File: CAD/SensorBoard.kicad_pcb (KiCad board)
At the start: 4 copper layers, 0 parts

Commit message: Begin initial PCB design
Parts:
- added C1: 4u7, Capacitor_SMD:C_0603_1608Metric, F.Cu at (112.5, 134.5)
- added C10: TODO, Capacitor_SMD:C_0402_1005Metric, F.Cu at (92.0, 134.2)
- added C11: TODO, Capacitor_SMD:C_0402_1005Metric, F.Cu at (92.0, 136.2)
- added C12: TODO, Capacitor_SMD:C_0402_1005Metric, F.Cu at (92.0, 138.2)
- added C13: TODO, Capacitor_SMD:C_0402_1005Metric, F.Cu at (92.0, 140.1)
- added C14: 100n, Capacitor_SMD:C_0402_1005Metric, F.Cu at (92.0, 142.1)
- added C15: 100n, Capacitor_SMD:C_0402_1005Metric, F.Cu at (94.8, 134.2)
- added C16: 100n, Capacitor_SMD:C_0402_1005Metric, F.Cu at (94.8, 136.2)
- added C17: 100n, Capacitor_SMD:C_0402_1005Metric, F.Cu at (94.8, 138.2)
- added C18: 100n, Capacitor_SMD:C_0402_1005Metric, F.Cu at (94.8, 140.1)
- added C19: 100n, Capacitor_SMD:C_0402_1005Metric, F.Cu at (94.8, 142.1)
- added C2: 4u7, Capacitor_SMD:C_0603_1608Metric, F.Cu at (112.5, 137.0)
- added C20: 100n, Capacitor_SMD:C_0402_1005Metric, F.Cu at (97.7, 134.2)
- added C21: 100n, Capacitor_SMD:C_0402_1005Metric, F.Cu at (97.7, 136.2)
- added C22: 100n, Capacitor_SMD:C_0402_1005Metric, F.Cu at (97.7, 138.2)
- added C23: 100n, Capacitor_SMD:C_0402_1005Metric, F.Cu at (97.7, 140.1)
- added C24: 100n, Capacitor_SMD:C_0402_1005Metric, F.Cu at (97.7, 142.1)
- added C3: 100n, Capacitor_SMD:C_0402_1005Metric, F.Cu at (89.1, 134.2)
- added C4: 100n, Capacitor_SMD:C_0402_1005Metric, F.Cu at (89.1, 136.2)
- added C5: 100n, Capacitor_SMD:C_0402_1005Metric, F.Cu at (89.1, 138.2)
- added C6: 100n, Capacitor_SMD:C_0402_1005Metric, F.Cu at (89.1, 140.1)
- added C7: 100n, Capacitor_SMD:C_0402_1005Metric, F.Cu at (89.1, 142.1)
- added C8: 4u7, Capacitor_SMD:C_0603_1608Metric, F.Cu at (112.5, 139.5)
- added C9: 4u7, Capacitor_SMD:C_0603_1608Metric, F.Cu at (112.5, 142.0)
- added D1: RED, LED_SMD:LED_0402_1005Metric, F.Cu at (167.0, 119.5)
- added D2: RED, LED_SMD:LED_0402_1005Metric, F.Cu at (169.0, 119.5)
- added D3: RED, LED_SMD:LED_0402_1005Metric, F.Cu at (171.0, 119.5)
- added D4: RED, LED_SMD:LED_0402_1005Metric, F.Cu at (173.0, 119.5)
- added D6: LED, LED_SMD:LED_0402_1005Metric, F.Cu at (144.0, 119.5)
- added D7: LED, LED_SMD:LED_0402_1005Metric, F.Cu at (144.0, 121.5)
- added D8: ASMT-YTB7-0AA02, LED_SMD:LED_Avago_PLCC6_3x2.8mm, F.Cu at (159.0, 121.5)
- added J1: USB C 2.0, Connector_USB:USB_C_Receptacle_GCT_USB4105-xx-A_16P_TopMnt_Horizontal, F.Cu at (126.8, 135.0)
- added J2: SWD Connector, SensorBoard:SM03B-SR, F.Cu at (186.9, 141.1)
- added J3: UART Connector, SensorBoard:SM03B-SR, F.Cu at (186.9, 129.0)
- added J4: DAC Connector, SensorBoard:SM02B-SR, F.Cu at (186.9, 135.0)
- added M1: M1, MountingHole:MountingHole_3.2mm_M3_Pad_Via, F.Cu at (128.5, 121.0)
- added M2: M2, MountingHole:MountingHole_3.2mm_M3_Pad_Via, F.Cu at (128.5, 149.0)
- added M3: M3, MountingHole:MountingHole_3.2mm_M3_Pad_Via, F.Cu at (186.5, 121.0)
- added M4: M4, MountingHole:MountingHole_3.2mm_M3_Pad_Via, F.Cu at (186.5, 149.0)
- added R1: TODO, Resistor_SMD:R_0402_1005Metric, F.Cu at (89.1, 118.3)
- added R10: 1k, Resistor_SMD:R_0402_1005Metric, F.Cu at (92.0, 120.3)
- added R11: TODO, Resistor_SMD:R_0402_1005Metric, F.Cu at (92.0, 122.3)
- added R12: 220, Resistor_SMD:R_0402_1005Metric, F.Cu at (92.0, 124.3)
- added R13: 5k1, Resistor_SMD:R_0402_1005Metric, F.Cu at (92.0, 126.3)
- added R14: 220, Resistor_SMD:R_0402_1005Metric, F.Cu at (92.0, 128.2)
- added R15: 220, Resistor_SMD:R_0402_1005Metric, F.Cu at (92.0, 130.2)
- added R16: 5k1, Resistor_SMD:R_0402_1005Metric, F.Cu at (92.0, 132.2)
- added R17: 220, Resistor_SMD:R_0402_1005Metric, F.Cu at (94.9, 118.3)
- added R18: 5k1, Resistor_SMD:R_0402_1005Metric, F.Cu at (94.9, 120.3)
- added R19: 220, Resistor_SMD:R_0402_1005Metric, F.Cu at (94.9, 122.3)
- added R2: TODO, Resistor_SMD:R_0402_1005Metric, F.Cu at (89.1, 120.3)
- added R20: 5k1, Resistor_SMD:R_0402_1005Metric, F.Cu at (94.9, 124.3)
- added R21: 220, Resistor_SMD:R_0402_1005Metric, F.Cu at (94.9, 126.3)
- added R22: 5k1, Resistor_SMD:R_0402_1005Metric, F.Cu at (94.9, 128.2)
- added R23: 220, Resistor_SMD:R_0402_1005Metric, F.Cu at (94.9, 130.2)
- added R24: 220, Resistor_SMD:R_0402_1005Metric, F.Cu at (94.9, 132.2)
- added R25: 220, Resistor_SMD:R_0402_1005Metric, F.Cu at (97.8, 118.3)
- added R26: 220, Resistor_SMD:R_0402_1005Metric, F.Cu at (97.8, 120.3)
- added R27: 220, Resistor_SMD:R_0402_1005Metric, F.Cu at (97.8, 122.3)
- added R28: 220, Resistor_SMD:R_0402_1005Metric, F.Cu at (97.8, 124.3)
- added R29: 220, Resistor_SMD:R_0402_1005Metric, F.Cu at (97.8, 126.3)
- added R3: 100, Resistor_SMD:R_0402_1005Metric, F.Cu at (89.1, 122.3)
- added R4: 100, Resistor_SMD:R_0402_1005Metric, F.Cu at (89.1, 124.3)
- added R5: 100, Resistor_SMD:R_0402_1005Metric, F.Cu at (89.1, 126.3)
- added R6: 100, Resistor_SMD:R_0402_1005Metric, F.Cu at (89.1, 128.2)
- added R7: 5k1, Resistor_SMD:R_0402_1005Metric, F.Cu at (89.1, 130.2)
- added R8: 5k1, Resistor_SMD:R_0402_1005Metric, F.Cu at (89.1, 132.2)
- added R9: 1k, Resistor_SMD:R_0402_1005Metric, F.Cu at (92.0, 118.3)
- added SW1: SW_1, Button_Switch_SMD:SW_Push_SPST_NO_Alps_SKRK, F.Cu at (155.1, 149.5)
- added SW2: SW_2, Button_Switch_SMD:SW_Push_SPST_NO_Alps_SKRK, F.Cu at (159.6, 149.5)
- added SW3: SW_3, Button_Switch_SMD:SW_Push_SPST_NO_Alps_SKRK, F.Cu at (164.0, 149.5)
- added SW4: SW_4, Button_Switch_SMD:SW_Push_SPST_NO_Alps_SKRK, F.Cu at (168.4, 149.5)
- added SW5: SW_BOOT, Button_Switch_SMD:SW_Push_SPST_NO_Alps_SKRK, F.Cu at (136.0, 126.0)
- added SW6: SW_RST, Button_Switch_SMD:SW_Push_SPST_NO_Alps_SKRK, F.Cu at (136.5, 143.5)
- added U1: STM32U073CCT6, Package_QFP:LQFP-48_7x7mm_P0.5mm, F.Cu at (160.0, 135.0)
- added U2: MIC5365, Package_TO_SOT_SMD:SOT-23-5, F.Cu at (147.1, 128.1)
- added U3: USBLC6-2SC6, Package_TO_SOT_SMD:SOT-23-6, F.Cu at (137.1, 135.0)
- added U4: BME680, SensorBoard:BME630, F.Cu at (173.0, 134.5)
- added U5: BMI323, SensorBoard:BMI323, F.Cu at (148.0, 135.5)
- added U6: TC1047, Package_TO_SOT_SMD:SOT-23, F.Cu at (172.1, 126.0)
- added X1: 32MHz, Crystal:Crystal_SMD_2016-4Pin_2.0x1.6mm, F.Cu at (169.8, 142.4)
- added X2: 32kHz768, Crystal:Crystal_SMD_2012-2Pin_2.0x1.2mm, F.Cu at (149.0, 142.5)
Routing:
- added copper zone on In1.Cu, net GND
- added copper zone on In2.Cu, net GND
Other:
- board outline added: 69.9 x 40 mm

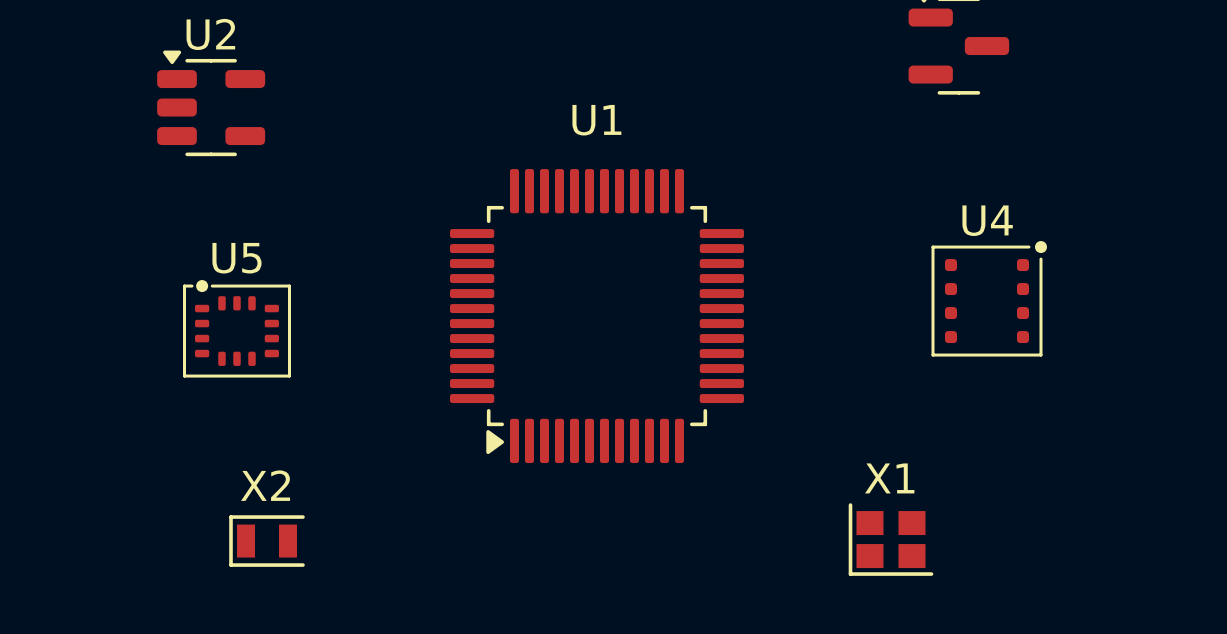
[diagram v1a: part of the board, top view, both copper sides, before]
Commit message: Add updates to footprints
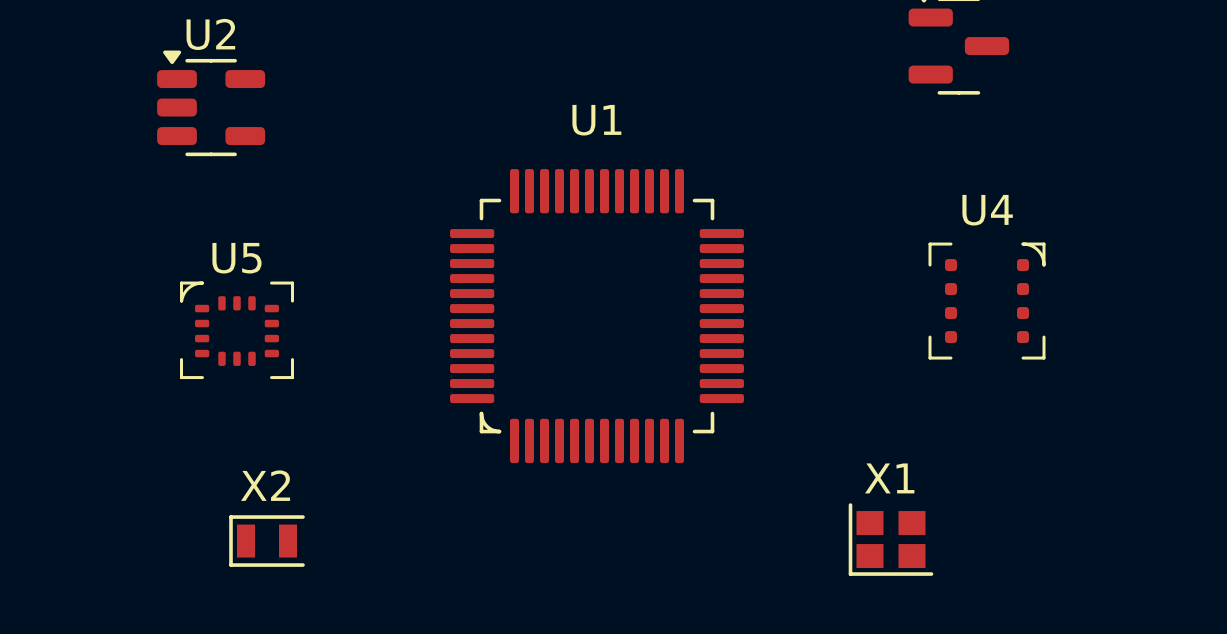
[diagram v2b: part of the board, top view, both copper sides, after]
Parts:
- U1: footprint Package_QFP:LQFP-48_7x7mm_P0.5mm -> SensorBoard:LQFP-48_7x7mm_P0.5mm
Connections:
- J1 pad A8: (no net) -> unconnected-(J1-SBU1-PadA8)
- J1 pad B8: (no net) -> unconnected-(J1-SBU2-PadB8)
- M1 pad 1: GND -> (no net)
- M2 pad 1: GND -> (no net)
- M3 pad 1: GND -> (no net)
- M4 pad 1: GND -> (no net)
- U5 pad 10: (no net) -> unconnected-(U5-NC-Pad10)
- U5 pad 11: (no net) -> unconnected-(U5-NC-Pad11)
- U5 pad 2: (no net) -> unconnected-(U5-NC-Pad2)
- U5 pad 3: (no net) -> unconnected-(U5-NC-Pad3)

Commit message: Update and add more footprints
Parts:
- D1, D2, D3, D4, D6, D7: footprint LED_SMD:LED_0402_1005Metric -> LED_SMD:LED_0805_2012Metric
- D8: footprint LED_SMD:LED_Avago_PLCC6_3x2.8mm -> SensorBoard:ASMT-YTB7-0AA02
- SW1, SW2, SW3, SW4, SW5, SW6: footprint Button_Switch_SMD:SW_Push_SPST_NO_Alps_SKRK -> SensorBoard:PTS636-SM25F-SMTR-LFS
- moved D8 4.12 mm to (155.7, 119.0)
- moved U2 3.50 mm to (150.1, 126.2)
- moved U5 2.00 mm to (148.0, 133.5)
- moved X2 1.72 mm to (150.6, 141.8)
- moved X1 1.59 mm to (168.8, 141.2)
- moved U4 1.52 mm to (174.5, 134.8)
- turned U1 to 135 degrees

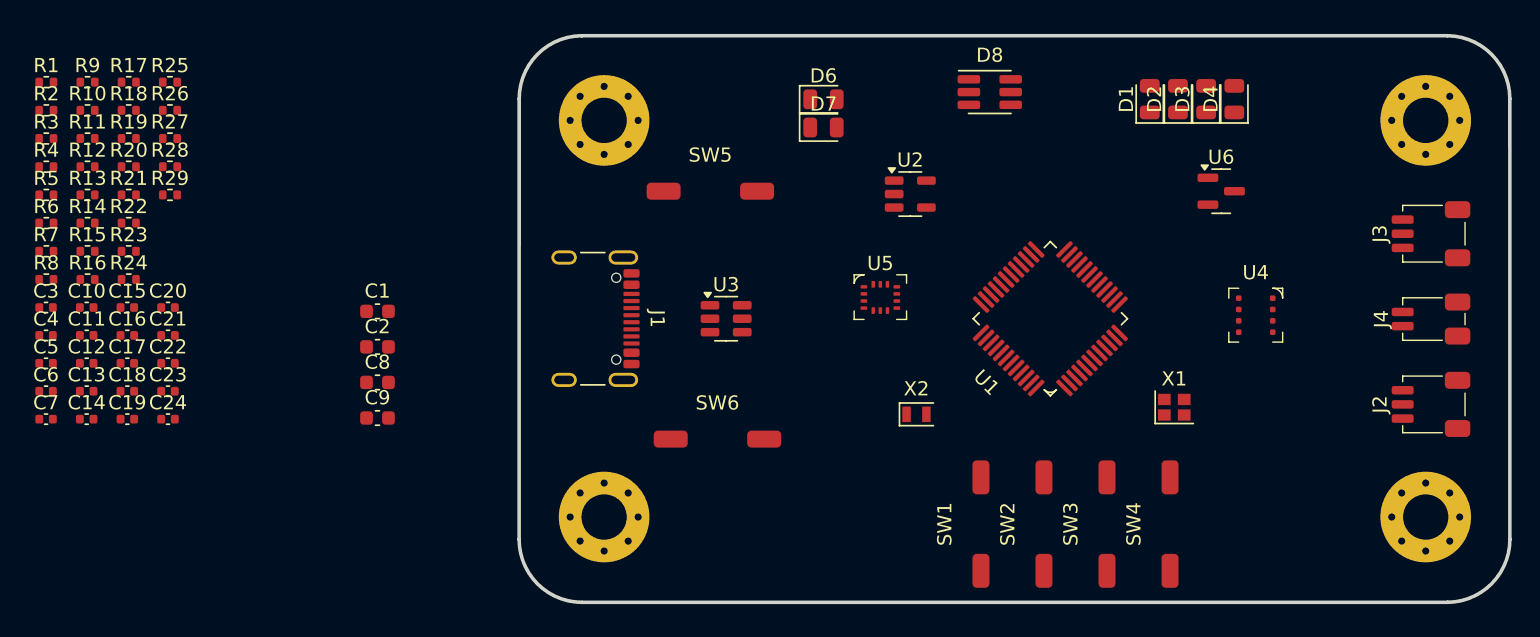
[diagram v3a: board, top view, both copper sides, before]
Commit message: Update oscillator footprint
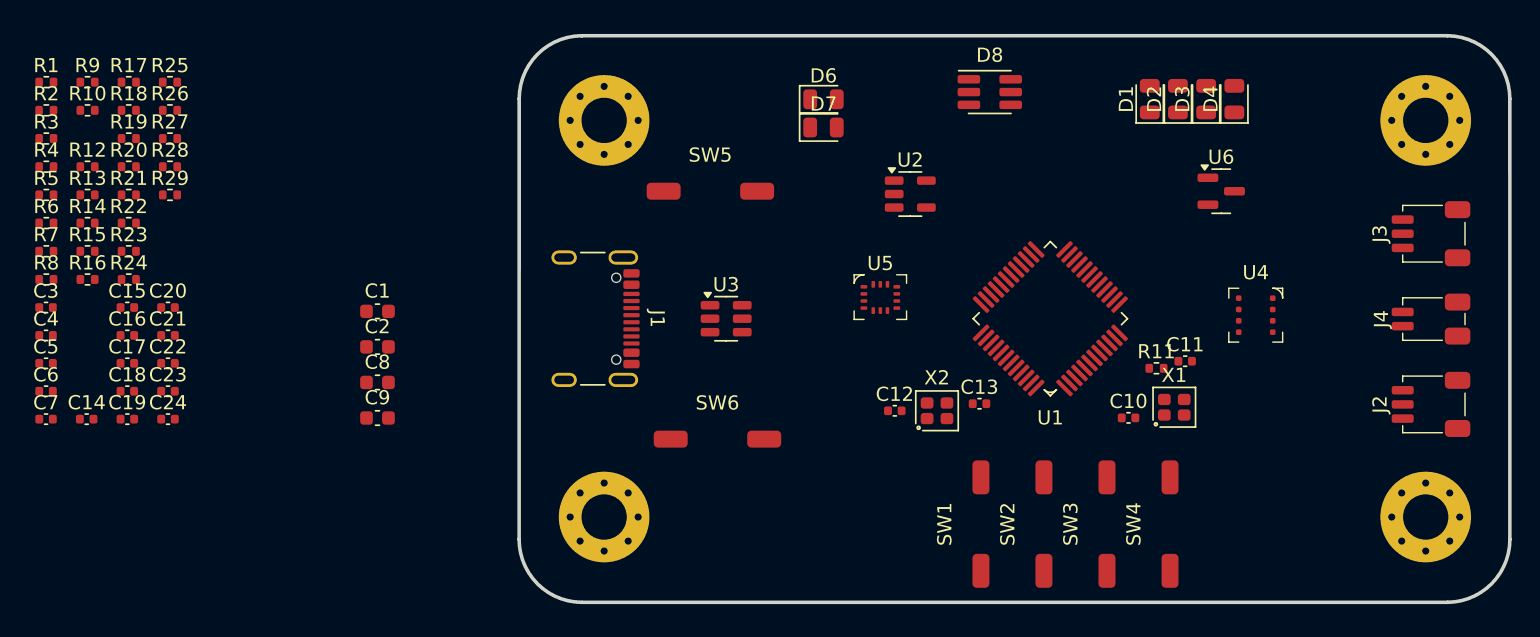
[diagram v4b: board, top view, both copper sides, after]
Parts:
- X1: footprint Crystal:Crystal_SMD_2016-4Pin_2.0x1.6mm -> SensorBoard:Crystal_SMD_2016-4Pin_2.0x1.6mm
- X2: footprint Crystal:Crystal_SMD_2012-2Pin_2.0x1.2mm -> SensorBoard:Crystal_SMD_2016-4Pin_2.0x1.6mm
- moved C11 77.6 mm to (169.5, 138.0)
- moved R11 77.2 mm to (167.5, 138.5)
- moved C10 74.0 mm to (165.5, 142.0)
- moved C13 63.0 mm to (155.0, 141.0)
- moved C12 57.1 mm to (149.0, 141.5)
- moved X2 1.47 mm to (152.0, 141.5)
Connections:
- X2 pad 2: LSE_OUT -> GND

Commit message: Finish rough components placement
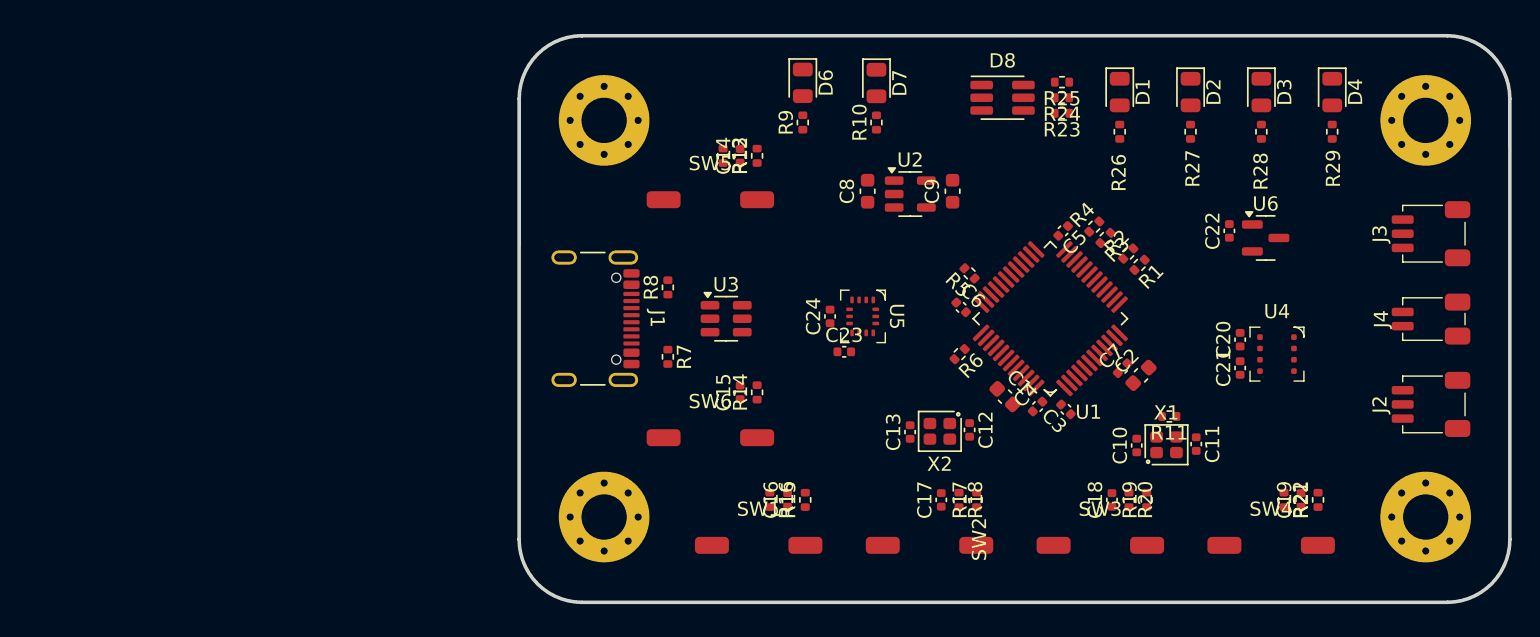
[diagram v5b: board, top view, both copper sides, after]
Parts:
- moved R21 86.7 mm to (178.9, 147.8), turned to 90 degrees
- moved R22 83.9 mm to (176.5, 147.8), turned to -90 degrees
- moved C19 83.1 mm to (177.7, 147.8), turned to 90 degrees
- moved R29 82.2 mm to (179.9, 121.8), turned to 90 degrees
- moved R1 78.3 mm to (166.3, 131.2), turned to -135 degrees
- moved R28 77.1 mm to (174.9, 121.8), turned to 90 degrees
- moved R2 77.0 mm to (165.5, 130.4), turned to -135 degrees
- moved R19 76.3 mm to (166.8, 147.8), turned to 90 degrees
- moved C7 76.1 mm to (165.1, 138.5), turned to 45 degrees
- moved C21 75.7 mm to (173.4, 138.5), turned to 90 degrees
- moved C20 75.7 mm to (173.4, 136.5), turned to 90 degrees
- moved C22 75.5 mm to (172.6, 128.8), turned to 90 degrees
- moved R3 75.1 mm to (163.9, 129.3), turned to -135 degrees
- moved R20 74.4 mm to (165.6, 147.8), turned to -90 degrees
- moved R4 74.1 mm to (163.1, 128.5), turned to 45 degrees
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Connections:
- net Net-(D6-A) renamed /+5V_LED
- net Net-(D7-A) renamed /+3V3_LED
- M1 pad 1: (no net) -> GND
- M2 pad 1: (no net) -> GND
- M3 pad 1: (no net) -> unconnected-(M3-Pad1)
- M4 pad 1: (no net) -> GND

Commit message: Add initial traces and vias
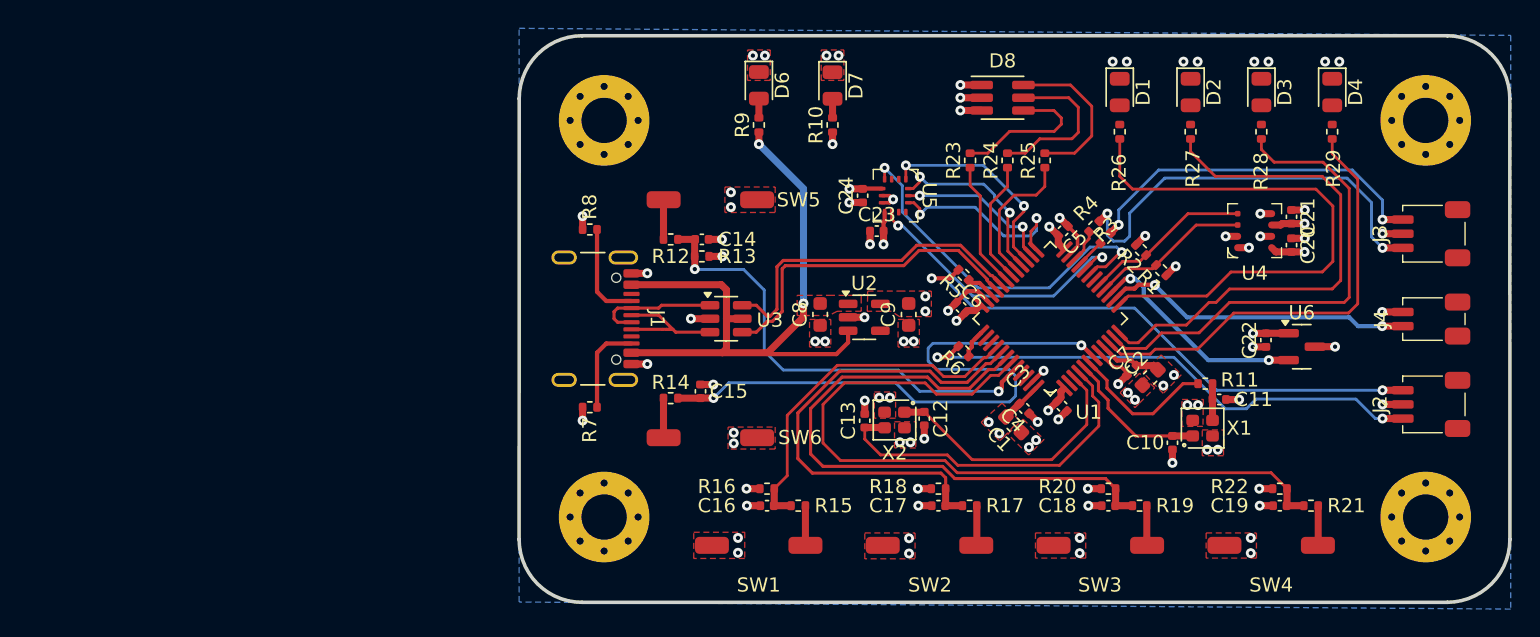
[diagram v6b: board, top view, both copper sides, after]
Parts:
- moved C21 11.3 mm to (177.0, 127.8), turned to -90 degrees
- moved C8 9.32 mm to (143.8, 134.7)
- moved U2 9.29 mm to (146.9, 134.9)
- moved C9 9.24 mm to (150.0, 134.7)
- moved U4 8.86 mm to (174.4, 128.8), turned to 180 degrees
- moved C23 8.83 mm to (147.8, 128.8)
- moved C24 8.83 mm to (146.8, 126.3)
- moved U5 8.83 mm to (149.1, 126.3)
- moved R12 8.49 mm to (133.2, 129.4), turned to 0 degrees
- moved C22 8.13 mm to (175.2, 136.5)
- moved U6 8.09 mm to (177.8, 137.0)
- moved C20 7.60 mm to (177.0, 129.8), turned to -90 degrees
- moved R23 7.29 mm to (154.3, 123.8), turned to 90 degrees
- moved R13 7.26 mm to (135.4, 130.6), turned to 0 degrees
- moved R8 6.86 mm to (127.5, 128.7), turned to 180 degrees
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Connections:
- M3 pad 1: unconnected-(M3-Pad1) -> GND
- U1 pad 10: LED_1 -> LED_4
- U1 pad 11: LED_2 -> LED_3
- U1 pad 12: LED_3 -> LED_2
- U1 pad 13: LED_4 -> LED_1
- U1 pad 29: LED_R -> LED_B
- U1 pad 31: LED_B -> LED_R
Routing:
- net BTN_4: track 0.00 -> 54.4 mm
- net GND: track 0.00 -> 53.5 mm, vias 0 -> 73
- net +5V: track 0.00 -> 47.4 mm, vias 0 -> 2
- net MCU_RST: track 0.00 -> 46.3 mm, vias 0 -> 2
- net BTN_3: track 0.00 -> 44.1 mm
- net LED_1: track 0.00 -> 38.8 mm
- net SWD_SWDIO: track 0.00 -> 38.7 mm, vias 0 -> 2
- net SWD_SWCLK: track 0.00 -> 37.0 mm, vias 0 -> 2
- net LED_2: track 0.00 -> 36.6 mm
- net BTN_2: track 0.00 -> 34.2 mm
- net LED_3: track 0.00 -> 34.1 mm
- net MCU_BOOT: track 0.00 -> 33.0 mm, vias 0 -> 2
- net LED_4: track 0.00 -> 31.7 mm
- net UART_RX: track 0.00 -> 29.6 mm, vias 0 -> 2
- net +3V3: track 0.00 -> 28.9 mm, vias 0 -> 28
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- added copper zone on B.Cu, net +3V3
- added copper zone on F.Cu, net +3V3
- added copper zone on F.Cu, net +5V
- added copper zone on F.Cu, net GND
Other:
- rule pad_to_mask_clearance: 0.08 -> 0
